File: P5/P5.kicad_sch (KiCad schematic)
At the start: 127 parts, among them J1 1-10, J2 Conn_01x10, J3 Conn_01x10, J4 Conn_01x10, J5 Conn_01x05, Q1 BC1, SW1 SW_Rotary1x3, SW10 SW_SPDT, SW11 SW_SPDT, SW12 SW_SPST, SW2 SW_SPDT, SW3 SW_SPDT, SW4 SW_Rotary1x3, SW5 SW_Rotary1x3, SW6 SW_Rotary1x3, SW7 SW_SPDT, SW8 SW_SPDT, SW8B1 SW_SPDT, SW9 SW_SPST, U1 TL072, U2 TL072, U3 LM741, U4 TL072, U5 4070, U6 4006, U7 LM741

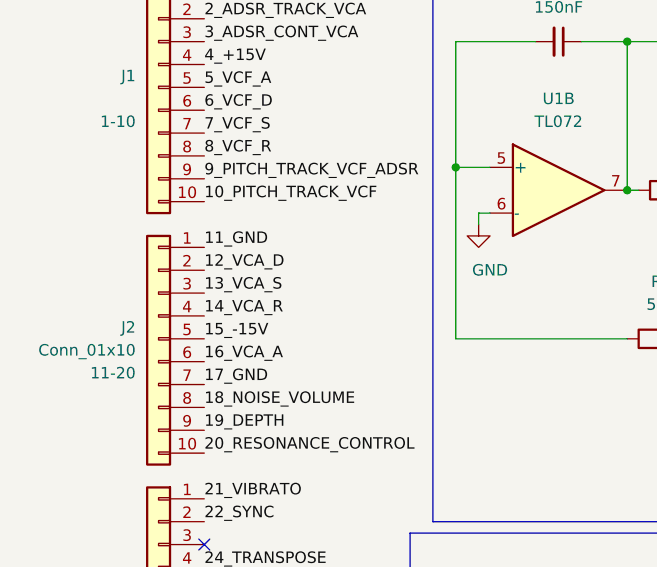
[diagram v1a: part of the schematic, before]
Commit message: Update P5 layout
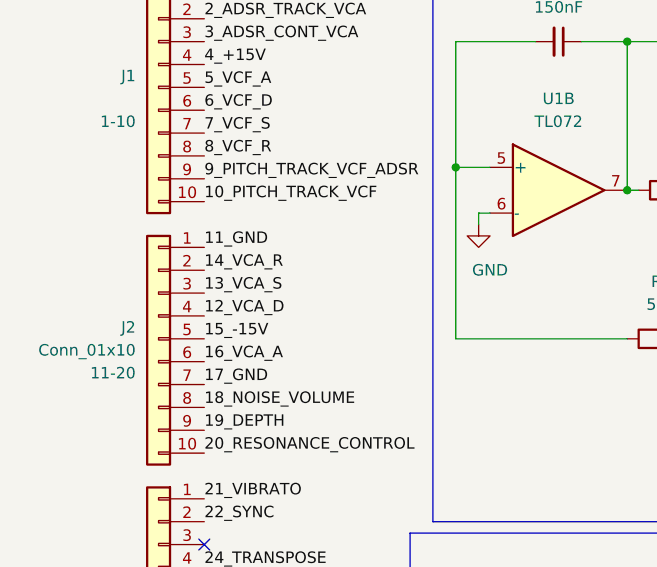
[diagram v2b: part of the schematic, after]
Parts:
- C15: footprint Capacitor_THT:CP_Radial_D5.0mm_P2.50mm -> Capacitor_THT:CP_Radial_D8.0mm_P5.00mm
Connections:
- net 12_VCA_D: now also J2.4 (Pin_4); no longer J2.2 (Pin_2)
- net 14_VCA_R: now also J2.2 (Pin_2); no longer J2.4 (Pin_4)
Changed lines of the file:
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@@
 	)
 	(label "12_VCA_D"
-		(at 31.75 45.72 0)
+		(at 31.75 50.8 0)
 		(effects
 			(font
@@
 	)
 	(label "14_VCA_R"
-		(at 31.75 50.8 0)
+		(at 31.75 45.72 0)
 		(effects
 			(font
@@
 			)
 		)
-		(property "Footprint" "Capacitor_THT:CP_Radial_D5.0mm_P2.50mm"
+		(property "Footprint" "Capacitor_THT:CP_Radial_D8.0mm_P5.00mm"
 			(at 396.24 63.5 0)
 			(effects
@@
 			)
 		)
-		(property "Datasheet" "~"
+		(property "Datasheet" ""
 			(at 396.24 63.5 0)
 			(effects

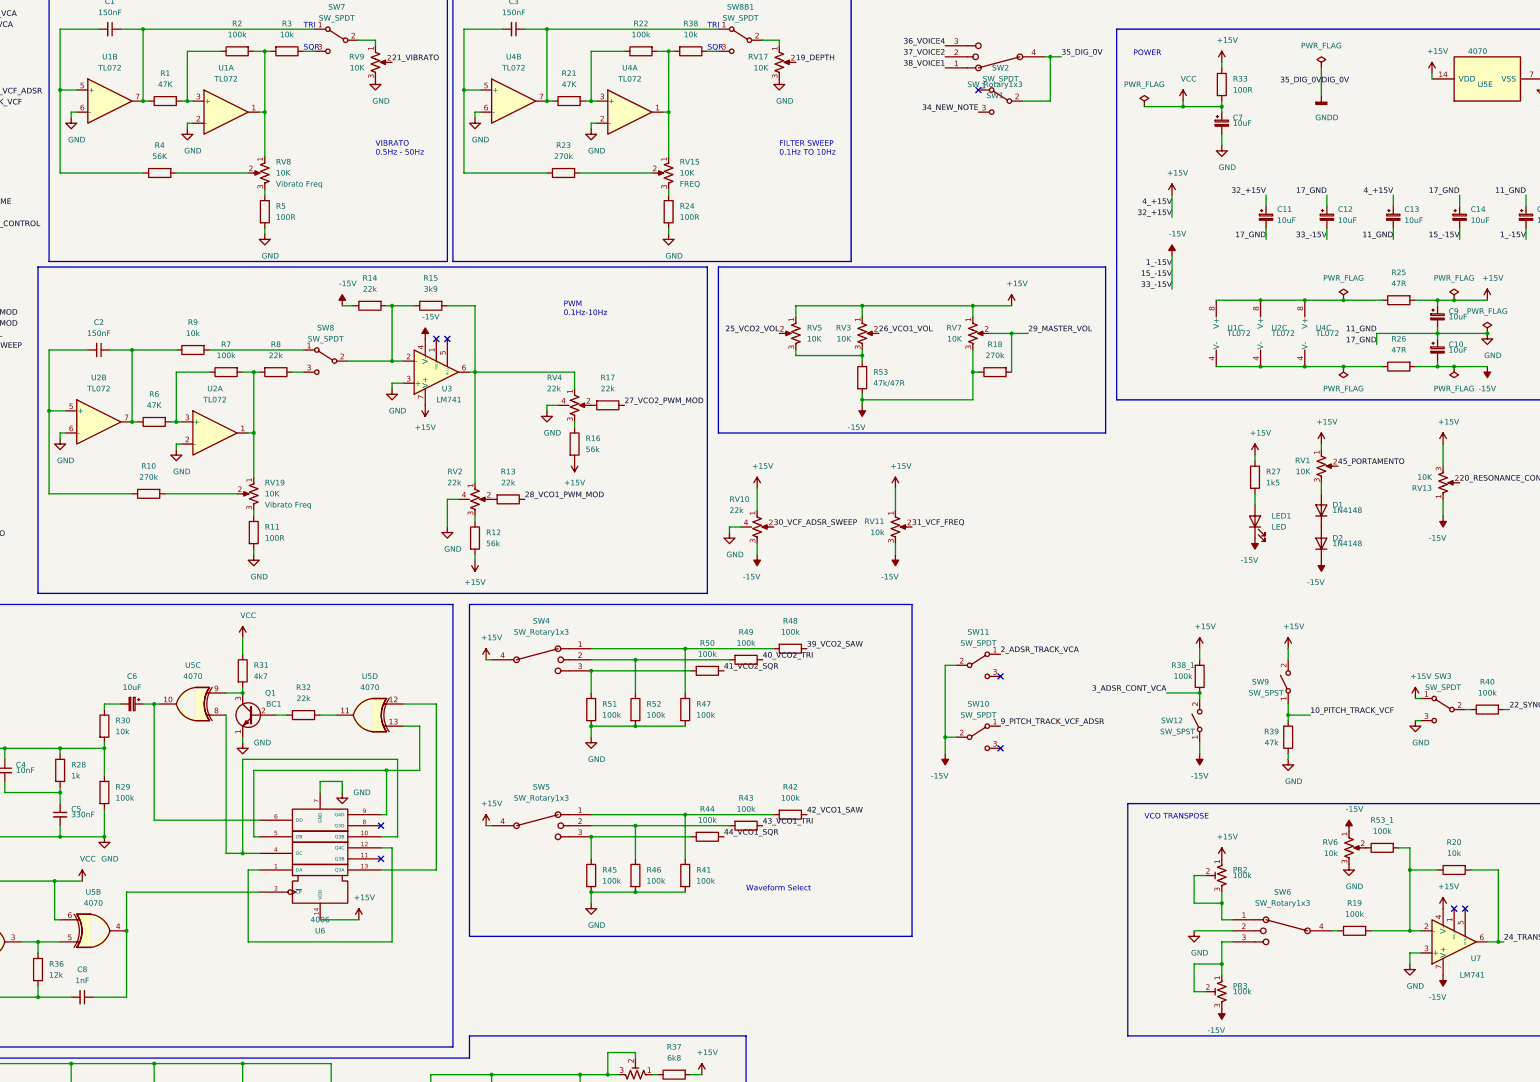
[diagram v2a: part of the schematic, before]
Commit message: Update P5 layout
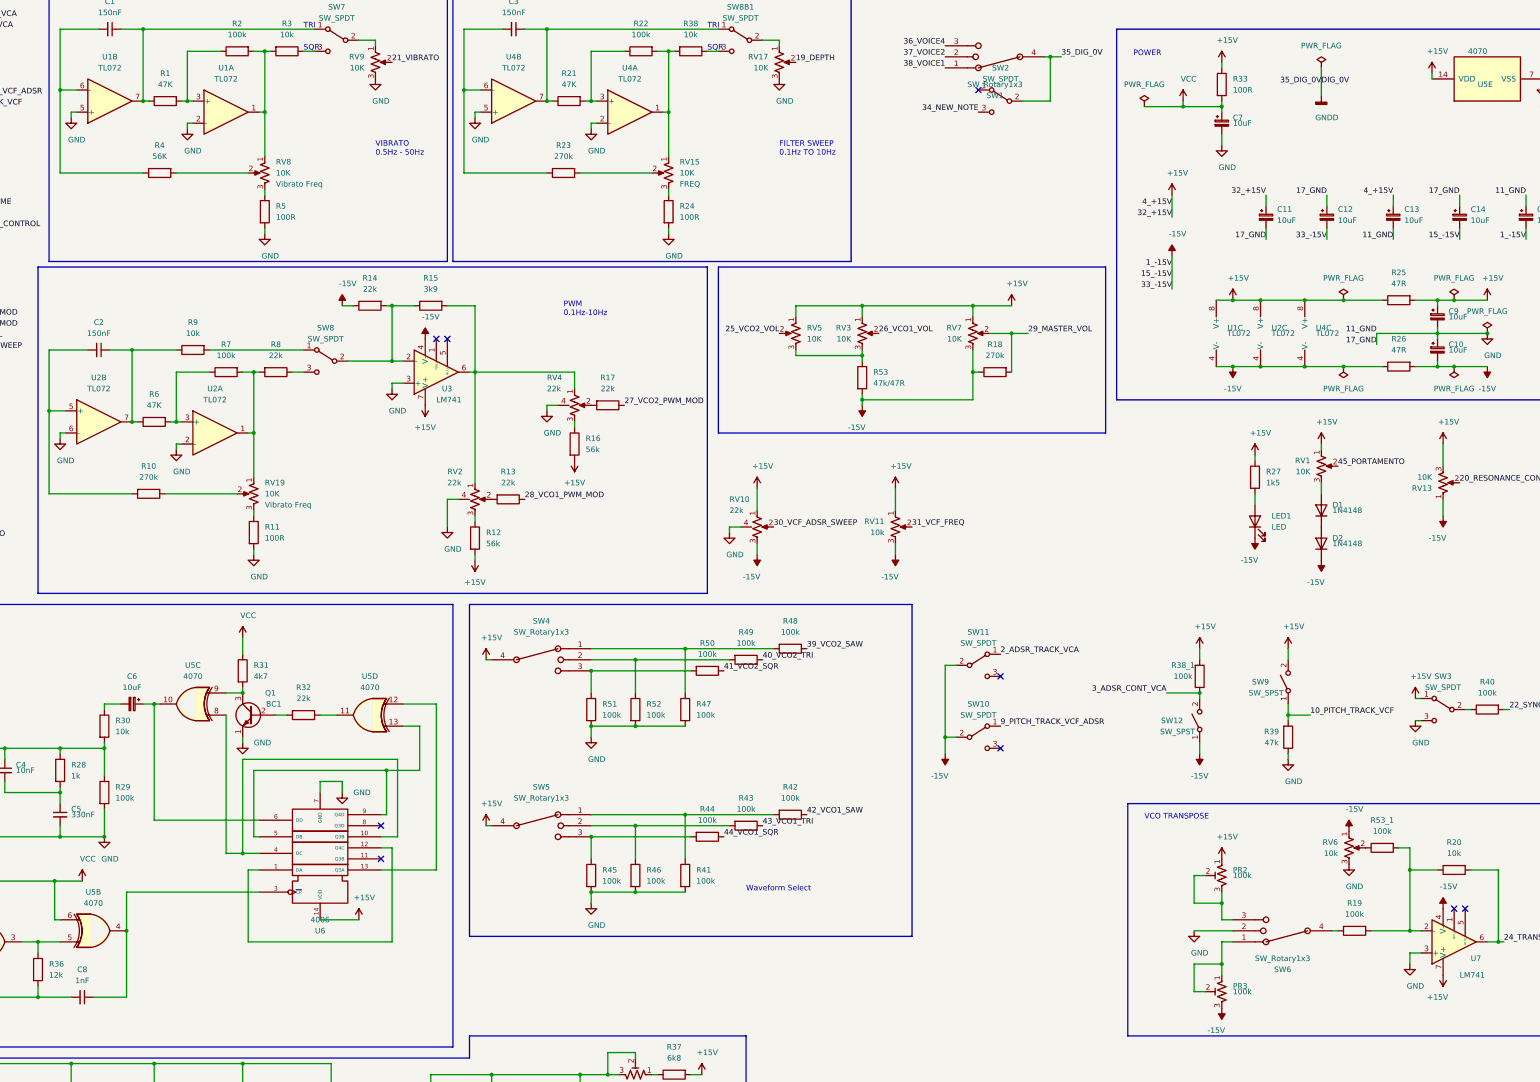
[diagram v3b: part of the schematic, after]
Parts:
- C10, C11, C12, C9: footprint Capacitor_THT:CP_Radial_D5.0mm_P2.50mm -> Capacitor_THT:CP_Radial_D8.0mm_P5.00mm
- C7: footprint Capacitor_THT:C_Rect_L7.0mm_W3.5mm_P2.50mm_P5.00mm -> Capacitor_THT:CP_Radial_D10.0mm_P5.00mm
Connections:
- net +15V: now also R25.1, U1.8 (V+), U2.8 (V+), U4.8 (V+), U7.7 (V+); no longer U7.4 (V-)
- net -15V: now also R26.1, U1.4 (V-), U2.4 (V-), U4.4 (V-), U7.4 (V-); no longer U7.7 (V+)
- net GND: now also U1.5 (+), U4.5 (+); no longer U1.6 (-), U4.6 (-)
- net at C1.2, R4.1: now also U1.6 (-); no longer U1.5 (+)
- net at C3.2, R23.1: now also U4.6 (-); no longer U4.5 (+)
- net at PR2.2, PR2.3: now also SW6.3; no longer SW6.1
- net at PR3.1, PR3.2: now also SW6.1; no longer SW6.3
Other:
- moved on the sheet: SW6
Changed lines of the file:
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@@
 	)
 	(junction
+		(at 328.93 97.79)
+		(diameter 0)
+		(color 0 0 0 0)
+	)
+	(junction
 		(at 269.24 99.06)
 		(diameter 0)
@@
 	)
 	(junction
+		(at 328.93 82.55)
+		(diameter 0)
+		(color 0 0 0 0)
+	)
+	(junction
 		(at 181.61 218.44)
 		(diameter 0)
@@
 	(wire
 		(pts
-			(xy 335.28 82.55) (xy 325.12 82.55)
+			(xy 335.28 82.55) (xy 328.93 82.55)
 		)
 		(stroke
@@
 	(wire
 		(pts
+			(xy 328.93 97.79) (xy 325.12 97.79)
+		)
+		(stroke
+			(width 0)
+			(type default)
+		)
+	)
+	(wire
+		(pts
 			(xy 148.59 134.62) (xy 148.59 128.27)
 		)
@@
 	(wire
 		(pts
+			(xy 328.93 82.55) (xy 325.12 82.55)
+		)
+		(stroke
+			(width 0)
+			(type default)
+		)
+	)
+	(wire
+		(pts
 			(xy 86.36 115.57) (xy 87.63 115.57)
 		)
@@
 	(wire
 		(pts
-			(xy 335.28 97.79) (xy 325.12 97.79)
+			(xy 335.28 97.79) (xy 328.93 97.79)
 		)
 		(stroke
@@
 		(lib_id "Amplifier_Operational:TL072")
 		(at 71.12 36.83 0)
+		(mirror x)
 		(unit 2)
 		(exclude_from_sim no)
@@
 		(on_board yes)
 		(dnp no)
+		(fields_autoplaced yes)
 		(property "Reference" "U1"
 			(at 71.12 26.67 0)
@@
 		(lib_id "Amplifier_Operational:TL072")
 		(at 163.83 36.83 0)
+		(mirror x)
 		(unit 2)
 		(exclude_from_sim no)
@@
 		(on_board yes)
 		(dnp no)
+		(fields_autoplaced yes)
 		(property "Reference" "U4"
 			(at 163.83 26.67 0)
@@
 			)
 		)
-		(property "Footprint" "Capacitor_THT:C_Rect_L7.0mm_W3.5mm_P2.50mm_P5.00mm"
+		(property "Footprint" "Capacitor_THT:CP_Radial_D10.0mm_P5.00mm"
 			(at 326.39 41.91 0)
 			(effects
@@
 			)
 		)
-		(property "Datasheet" "~"
+		(property "Datasheet" ""
 			(at 326.39 41.91 0)
 			(effects
@@
 	(symbol
 		(lib_id "P5:SW_Rotary1x3")
-		(at 341.63 227.33 0)
-		(mirror y)
+		(at 341.63 227.33 180)
 		(unit 1)
 		(exclude_from_sim no)
@@
 		(dnp no)
 		(property "Reference" "SW6"
-			(at 340.36 218.44 0)
+			(at 340.36 236.22 0)
 			(effects
 				(font
@@
 		)
 		(property "Value" "SW_Rotary1x3"
-			(at 340.36 220.98 0)
+			(at 340.36 233.68 0)
 			(effects
 				(font
@@
 		)
 		(property "Footprint" "P5:SR2612F-0304-18R0B-D8-N"
-			(at 344.17 219.71 0)
+			(at 344.17 234.95 0)
 			(effects
 				(font
@@
 		)
 		(property "Datasheet" "http://cdn-reichelt.de/documents/datenblatt/C200/DS-Serie%23LOR.pdf"
-			(at 344.17 219.71 0)
+			(at 344.17 234.95 0)
 			(effects
 				(font
@@
 	(symbol
 		(lib_id "power:-15V")
-		(at 377.19 237.49 180)
+		(at 377.19 222.25 0)
 		(unit 1)
 		(exclude_from_sim no)
@@
 		(dnp no)
 		(property "Reference" "#PWR0152"
-			(at 377.19 240.03 0)
+			(at 377.19 219.71 0)
 			(effects
 				(font
@@
 		)
 		(property "Value" "-15V"
-			(at 375.92 242.57 0)
+			(at 378.46 217.17 0)
 			(effects
 				(font
@@
 		)
 		(property "Footprint" ""
-			(at 377.19 237.49 0)
+			(at 377.19 222.25 0)
 			(effects
 				(font
@@
 		)
 		(property "Datasheet" ""
-			(at 377.19 237.49 0)
+			(at 377.19 222.25 0)
 			(effects
 				(font
@@
 		)
 		(property "Description" ""
-			(at 377.19 237.49 0)
+			(at 377.19 222.25 0)
 			(effects
 				(font
@@
 	(symbol
 		(lib_id "power:+15V")
-		(at 377.19 222.25 0)
+		(at 377.19 237.49 180)
 		(unit 1)
 		(exclude_from_sim no)
@@
 		(dnp no)
 		(property "Reference" "#PWR0153"
-			(at 377.19 226.06 0)
+			(at 377.19 233.68 0)
 			(effects
 				(font
@@
 		)
 		(property "Value" "+15V"
-			(at 378.46 217.17 0)
+			(at 375.92 242.57 0)
 			(effects
 				(font
@@
 		)
 		(property "Footprint" ""
-			(at 377.19 222.25 0)
+			(at 377.19 237.49 0)
 			(effects
 				(font
@@
 		)
 		(property "Datasheet" ""
-			(at 377.19 222.25 0)
+			(at 377.19 237.49 0)
 			(effects
 				(font
@@
 		)
 		(property "Description" ""
-			(at 377.19 222.25 0)
+			(at 377.19 237.49 0)
 			(effects
 				(font
@@
 			)
 		)
-		(property "Footprint" "Capacitor_THT:CP_Radial_D5.0mm_P2.50mm"
+		(property "Footprint" "Capacitor_THT:CP_Radial_D8.0mm_P5.00mm"
 			(at 375.92 86.36 0)
 			(effects
@@
 			)
 		)
-		(property "Datasheet" "~"
+		(property "Datasheet" ""
 			(at 375.92 86.36 0)
 			(effects
@@
 			)
 		)
-		(property "Footprint" "Capacitor_THT:CP_Radial_D5.0mm_P2.50mm"
+		(property "Footprint" "Capacitor_THT:CP_Radial_D8.0mm_P5.00mm"
 			(at 375.92 93.98 0)
 			(effects
@@
 			)
 		)
-		(property "Datasheet" "~"
+		(property "Datasheet" ""
 			(at 375.92 93.98 0)
 			(effects
@@
 			)
 		)
-		(property "Footprint" "Capacitor_THT:CP_Radial_D5.0mm_P2.50mm"
+		(property "Footprint" "Capacitor_THT:CP_Radial_D8.0mm_P5.00mm"
 			(at 336.55 63.5 0)
 			(effects
@@
 			)
 		)
-		(property "Datasheet" "~"
+		(property "Datasheet" ""
 			(at 336.55 63.5 0)
 			(effects
@@
 	)
 	(symbol
+		(lib_id "power:+15V")
+		(at 328.93 82.55 0)
+		(unit 1)
+		(exclude_from_sim no)
+		(in_bom yes)
+		(on_board yes)
+		(dnp no)
+		(property "Reference" "#PWR01"
+			(at 328.93 86.36 0)
+			(effects
+				(font
+					(size 1.27 1.27)
+				)
+				(hide yes)
+			)
+		)
+		(property "Value" "+15V"
+			(at 330.2 77.47 0)
+			(effects
+				(font
+					(size 1.27 1.27)
+				)
+			)
+		)
+		(property "Footprint" ""
+			(at 328.93 82.55 0)
+			(effects
+				(font
+					(size 1.27 1.27)
+				)
+				(hide yes)
+			)
+		)
+		(property "Datasheet" ""
+			(at 328.93 82.55 0)
+			(effects
+				(font
+					(size 1.27 1.27)
+				)
+				(hide yes)
+			)
+		)
+		(property "Description" ""
+			(at 328.93 82.55 0)
+			(effects
+				(font
+					(size 1.27 1.27)
+				)
+			)
+		)
+		(pin "1"
+		)
+		(instances
+			(project "P5"
+				(path "/ea4598ea-5853-40f6-8351-3048776a4653"
+					(reference "#PWR01")
+					(unit 1)
+				)
+			)
+		)
+	)
+	(symbol
 		(lib_id "Device:C_Polarized_Small")
 		(at 365.76 63.5 0)
@@
 			)
 		)
-		(property "Footprint" "Capacitor_THT:CP_Radial_D5.0mm_P2.50mm"
+		(property "Footprint" "Capacitor_THT:CP_Radial_D8.0mm_P5.00mm"
 			(at 350.52 63.5 0)
 			(effects
@@
 			)
 		)
-		(property "Datasheet" "~"
+		(property "Datasheet" ""
 			(at 350.52 63.5 0)
 			(effects
@@
 					(unit 1)
 				)
+			)
+		)
+	)
+	(symbol
+		(lib_id "power:-15V")
+		(at 328.93 97.79 180)
+		(unit 1)
+		(exclude_from_sim no)
+		(in_bom yes)
+		(on_board yes)
+		(dnp no)
+		(property "Reference" "#PWR02"
+			(at 328.93 100.33 0)
+			(effects
+				(font
+					(size 1.27 1.27)
+				)
+				(hide yes)
+			)
+		)
+		(property "Value" "-15V"
+			(at 328.93 102.87 0)
+			(effects
+				(font
+					(size 1.27 1.27)
+				)
+			)
+		)
+		(property "Footprint" ""
+			(at 328.93 97.79 0)
+			(effects
+				(font
+					(size 1.27 1.27)
+				)
+				(hide yes)
+			)
+		)
+		(property "Datasheet" ""
+			(at 328.93 97.79 0)
+			(effects
+				(font
+					(size 1.27 1.27)
+				)
+				(hide yes)
+			)
+		)
+		(property "Description" ""
+			(at 328.93 97.79 0)
+			(effects
+				(font
+					(size 1.27 1.27)
+				)
+			)
+		)
+		(pin "1"
+		)
+		(instances
+			(project "P5"
+				(path "/ea4598ea-5853-40f6-8351-3048776a4653"
+					(reference "#PWR02")
+					(unit 1)
+				)

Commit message: Finish P5 layout
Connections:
- net VCC is gone; now on net +15V: C7.1, R31.1, R33.2, U5.1, U5.6
